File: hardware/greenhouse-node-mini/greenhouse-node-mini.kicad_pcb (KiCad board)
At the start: 4 copper layers, 70 x 50 mm, 43 parts, among them J1 Molex_KK_396_1x2, J2 JST_XH_2.54mm_1x2, J3 Conn_01x05_Female, J4 Molex_KK_396_1x2, J5 JST_XH_2.54mm_1x4, SW1 SW_Push, U1 ATtiny84A-P, U2 L7805, U3 PCF8574, U4 L298HN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

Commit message: Add power in/out silkscreen text
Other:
- board text added: "OUT"
- board text added: "VCC"
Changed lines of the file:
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@@
   (gr_line locked (start 129.5 43) (end 129.5 74) (layer "User.1") (width 0.15))
   (gr_line locked (start 72 74) (end 129.5 74) (layer "User.1") (width 0.15))
+  (gr_text "OUT" (at 94.1 39.6 270) (layer "F.SilkS")
+    (effects (font (size 1 1) (thickness 0.15)))
+  )
   (gr_text "Nick Bolton" (at 134.366 61.849 90) (layer "F.SilkS")
     (effects (font (size 1 1) (thickness 0.15)))
   )
+  (gr_text "VCC" (at 74.9 39.1) (layer "F.SilkS")
+    (effects (font (size 1 1) (thickness 0.15)))
+  )

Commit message: Add + pin text to PCB
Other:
- board text added: "+"
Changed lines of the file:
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@@
+    (effects (font (size 1 1) (thickness 0.15)))
+  )
+  (gr_text "+" (at 78.55 37.8) (layer "F.SilkS")
     (effects (font (size 1 1) (thickness 0.15)))
   )

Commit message: Change radio and MCU to STM32 + RFM69HW
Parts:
- added U6: STM32F030F4Px, Package_SO:TSSOP-20_4.4x6.5mm_P0.65mm, F.Cu at (44.6, 65.0)
- added U7: RFM69HW, Nick:HopeRF_RFM69HW, F.Cu at (51.4, 52.2)
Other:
- board text added: "Greenhouse Node Mini - Rev 2"
- board text removed: "Greenhouse Node Mini"

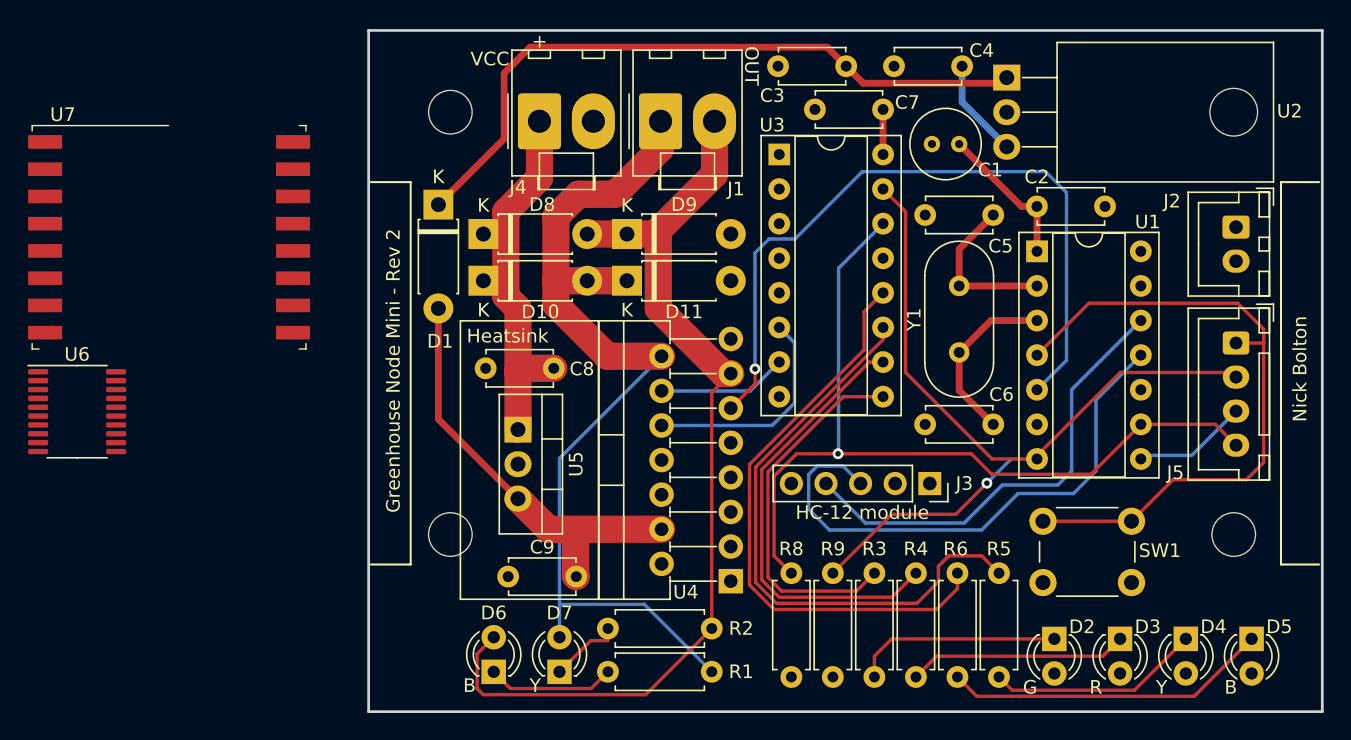
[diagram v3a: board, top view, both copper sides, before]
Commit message: Update PCB for node mini
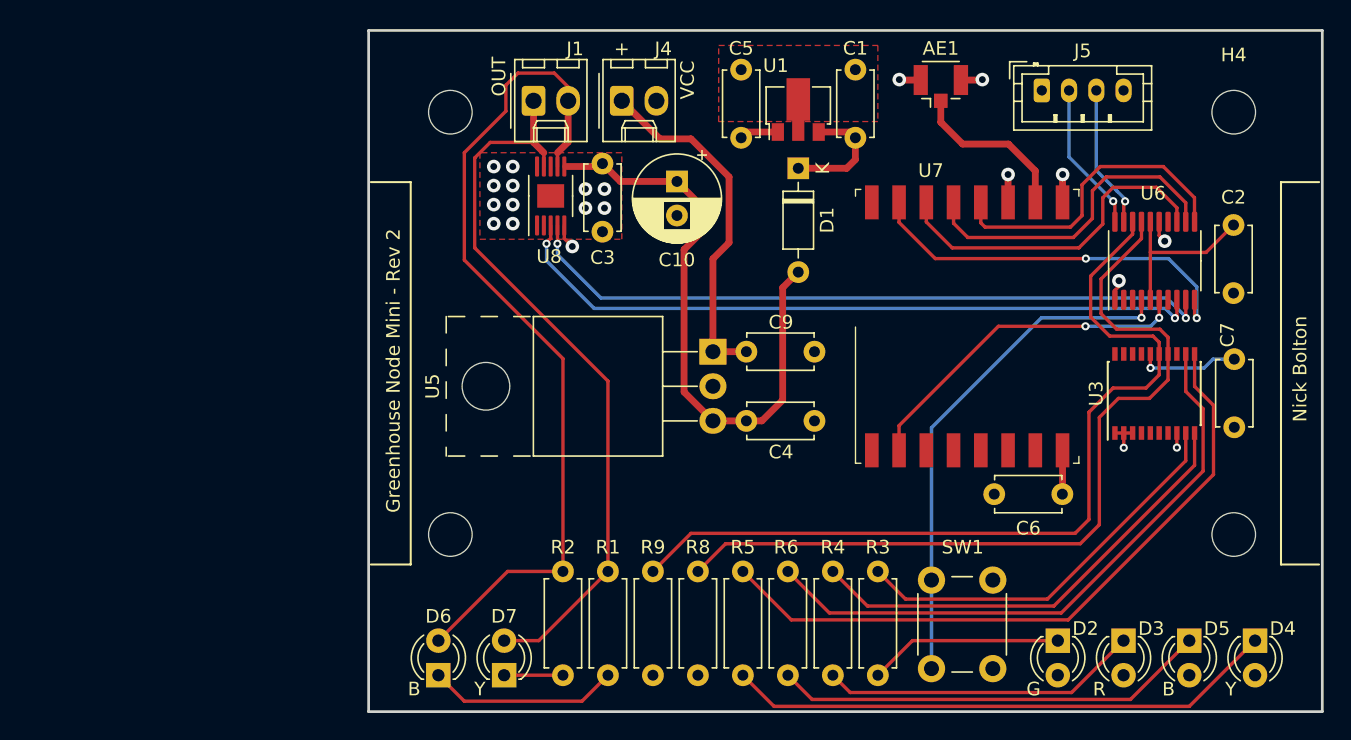
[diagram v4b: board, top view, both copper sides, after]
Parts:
- removed C8: 330nF, Capacitor_THT:C_Disc_D4.7mm_W2.5mm_P5.00mm
- removed D10, D11, D8, D9: 1N4001, Diode_THT:D_DO-41_SOD81_P7.62mm_Horizontal
- removed J2: JST_XH_2.54mm_1x2, Connector_JST:JST_XH_B2B-XH-A_1x02_P2.50mm_Vertical
- removed J3: Conn_01x05_Female, Connector_PinSocket_2.54mm:PinSocket_1x05_P2.54mm_Vertical
- removed U2: L7805, Package_TO_SOT_THT:TO-220-3_Horizontal_TabDown
- removed U4: L298HN, Package_TO_SOT_THT:TO-220-15_P2.54x2.54mm_StaggerOdd_Lead4.58mm_Vertical
- removed Y1: 8MHz, Crystal:Crystal_HC49-4H_Vertical
- added AE1: U.FL-R-SMT-1, Connector_Coaxial:U.FL_Hirose_U.FL-R-SMT-1_Vertical, F.Cu at (108.0, 41.1)
- added C10: 100uF, Capacitor_THT:CP_Radial_D6.3mm_P2.50mm, F.Cu at (88.6, 48.1)
- added H4: MountingHole, MountingHole:MountingHole_3.2mm_M3, F.Cu at (129.5, 43.0)
- added U8: A4952ELYTR-T, Package_SO:MSOP-10-1EP_3x3mm_P0.5mm_EP1.73x1.98mm, F.Cu at (79.4, 49.1)
- C1: value 100uF -> 100nF; footprint Capacitor_THT:C_Radial_D5.0mm_H7.0mm_P2.00mm -> Capacitor_THT:C_Disc_D4.7mm_W2.5mm_P5.00mm
- C2: value 10nF -> 100nF
- C3: value 330nF -> 220nF
- C5: value 22pF -> 100nF
- C6: value 22pF -> 10nF
- D1: value 1N4001 -> BAT46; footprint Diode_THT:D_DO-41_SOD81_P7.62mm_Horizontal -> Diode_THT:D_DO-35_SOD27_P7.62mm_Horizontal
- J1, J4: value Molex_KK_396_1x2 -> Conn_01x02_Pin; footprint Connector_Molex:Molex_KK-396_A-41791-0002_1x02_P3.96mm_Vertical -> Connector_Molex:Molex_KK-254_AE-6410-02A_1x02_P2.54mm_Vertical
- J5: value JST_XH_2.54mm_1x4 -> Conn_01x04_Pin; footprint Connector_JST:JST_XH_B4B-XH-A_1x04_P2.50mm_Vertical -> Connector_JST:JST_PH_B4B-PH-K_1x04_P2.00mm_Vertical
- U1: value ATtiny84A-P -> XC6706x; footprint Package_DIP:DIP-14_W7.62mm_Socket -> Package_TO_SOT_SMD:SOT-89-3
- U3: value PCF8574 -> PCF8574ATS/3,118; footprint Package_DIP:DIP-16_W7.62mm_Socket -> Package_SO:SSOP-20_4.4x6.5mm_P0.65mm
- U5: footprint Package_TO_SOT_THT:TO-220-3_Vertical -> Package_TO_SOT_THT:TO-220-3_Horizontal_TabUp
- U6: value STM32F030F4Px -> STM32F030F4P6
- moved U6 79.9 mm to (123.7, 53.9), turned to 90 degrees
- moved U7 58.9 mm to (109.9, 58.7), turned to 90 degrees
- moved U3 32.7 mm to (123.7, 63.6), turned to 90 degrees
- moved C7 31.6 mm to (129.5, 61.1), turned to -90 degrees
- moved D1 26.6 mm to (97.5, 47.1)
- moved C4 23.6 mm to (98.7, 60.6)
- moved J5 23.4 mm to (115.4, 41.4), turned to 0 degrees
- moved U1 20.5 mm to (97.5, 42.5), turned to 90 degrees
- moved C5 19.4 mm to (93.3, 44.9), turned to 90 degrees
- moved R5 18.8 mm to (93.5, 76.7)
- moved C9 16.9 mm to (93.7, 65.7), turned to 0 degrees
- moved U5 15.4 mm to (91.3, 60.6)
- moved C3 14.7 mm to (83.2, 46.8), turned to -90 degrees
- moved C2 14.5 mm to (129.5, 51.3), turned to -90 degrees
- moved SW1 13.6 mm to (107.3, 83.8), turned to 90 degrees
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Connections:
- C1 pad 1: +5V -> GND
- C1 pad 2: GND -> Net-(D1-K)
- C2 pad 1: +5V -> +3V3
- C3 pad 1: GND -> +10V
- C3 pad 2: Net-(D1-K) -> GND
- C4 pad 1: +5V -> GND
- C4 pad 2: GND -> Net-(J4-Pin_1)
- C5 pad 1: /XTAL1 -> +3V3
- C6 pad 1: /XTAL2 -> +3V3
- C7 pad 1: +5V -> +3V3
- D2 pad 2: +5V -> +3V3
- D3 pad 2: +5V -> +3V3
- D4 pad 2: +5V -> +3V3
- D5 pad 2: +5V -> +3V3
- J4 pad 1: +12V -> Net-(J4-Pin_1)
- J5 pad 1: /Reset -> +3V3
- J5 pad 2: /PGM_A -> /SWCLK
- J5 pad 3: /PGM_B -> /SWDIO
- J5 pad 4: /PGM_C -> GND
- R8 pad 1: +5V -> +3V3
- R8 pad 2: /PGM_C -> /SCL
- R9 pad 1: +5V -> +3V3
- R9 pad 2: /PGM_A -> /SDA
- SW1 pad 1: /Reset -> /RST
- U1 pad 1: +5V -> +3V3
- U1 pad 2: /XTAL1 -> GND
- U1 pad 3: /XTAL2 -> Net-(D1-K)
- U3 pad 14: /PGM_C -> /SCL
- U3 pad 15: /PGM_A -> /SDA
- U3 pad 16: +5V -> +3V3
- U3 pad 6: /M_IN1 -> unconnected-(U3-P2-Pad6)
- U3 pad 7: /M_IN2 -> unconnected-(U3-P3-Pad7)
- U5 pad 1: +12V -> Net-(J4-Pin_1)
- U6 pad 1: unconnected-(U6-BOOT0-Pad1) -> GND
- U6 pad 10: unconnected-(U6-PA4-Pad10) -> /RM_CS
- U6 pad 11: unconnected-(U6-PA5-Pad11) -> /SCK
- U6 pad 12: unconnected-(U6-PA6-Pad12) -> /MISO
- U6 pad 13: unconnected-(U6-PA7-Pad13) -> /MOSI
- U6 pad 15: unconnected-(U6-VSS-Pad15) -> GND
- U6 pad 16: unconnected-(U6-VDD-Pad16) -> +3V3
- U6 pad 17: unconnected-(U6-PA9-Pad17) -> /SCL
- U6 pad 18: unconnected-(U6-PA10-Pad18) -> /SDA
- U6 pad 19: unconnected-(U6-PA13-Pad19) -> /SWDIO
- U6 pad 20: unconnected-(U6-PA14-Pad20) -> /SWCLK
- U6 pad 4: unconnected-(U6-NRST-Pad4) -> /RST
- U6 pad 5: unconnected-(U6-VDDA-Pad5) -> +3V3
- U6 pad 6: unconnected-(U6-PA0-Pad6) -> /RM_IRQ
- U6 pad 8: unconnected-(U6-PA2-Pad8) -> /M_IN2
- U6 pad 9: unconnected-(U6-PA3-Pad9) -> /M_IN1
- U7 pad 10: unconnected-(U7-ANA-Pad10) -> Net-(AE1-A)
- U7 pad 11: Net-(U7-GND-Pad11) -> GND
- U7 pad 12: unconnected-(U7-SCK-Pad12) -> /SCK
- U7 pad 13: unconnected-(U7-MISO-Pad13) -> /MISO
- U7 pad 14: unconnected-(U7-MOSI-Pad14) -> /MOSI
- U7 pad 15: unconnected-(U7-NSS-Pad15) -> /RM_CS
- U7 pad 2: unconnected-(U7-DIO0-Pad2) -> /RM_IRQ
- U7 pad 8: unconnected-(U7-3.3V-Pad8) -> +3V3
- U7 pad 9: Net-(U7-GND-Pad11) -> GND
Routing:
- net /SDA: track 0.00 -> 64.2 mm
- net /PGM_C: track 63.3 -> 0.00 mm, vias 1 -> 0
- net /PGM_A: track 62.1 -> 0.00 mm, vias 1 -> 0
- net /SCL: track 0.00 -> 61.7 mm
- net /M_EN: track 53.5 -> 0.00 mm, vias 1 -> 0
- net /Reset: track 48.8 -> 0.00 mm
- net /M_IN2: track 9.51 -> 52.0 mm, vias 0 -> 2
- net Net-(D1-K): track 50.6 -> 8.92 mm
- net /RAD_RX: track 40.5 -> 0.00 mm
- net /RST: track 0.00 -> 37.8 mm, vias 0 -> 1
- net /M_IN1: track 16.5 -> 51.6 mm, vias 0 -> 2
- net /RAD_TX: track 34.0 -> 0.00 mm
- net /RM_CS: track 0.00 -> 29.0 mm, vias 0 -> 2
- net +3V3: track 0.00 -> 28.0 mm, vias 0 -> 2
- net +12V: track 26.7 -> 0.00 mm
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- added copper zone on In2.Cu, net +3V3
- added copper zone on F.Cu, net GND
- removed copper zone on In2.Cu, net +5V
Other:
- board text removed: "HC-12 module"
